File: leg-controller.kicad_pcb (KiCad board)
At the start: 2 copper layers, 99.8 x 77.5 mm, 103 parts, among them J1 Power, J10 Motor, J11 Rotary_Encoder, J12 Conn_01x02, J13 USB_B_Mini, J14 ISP, J15 Motor_E, J16 Motor_D, J17 Motor_F, J18 Conn_01x02, J19 Conn_01x02, J2 I2C, J3 Conn_02x01, J4 Motor, J5 Rotary_Encoder, J6 Conn_02x01, J7 Motor, J8 Rotary_Encoder, J9 Conn_02x01, Q1 Q_NPN_BEC, Q2 SiSS05DN, Q3 Q_NPN_BEC, Q4 SiSS05DN, Q5 Q_NPN_BEC, Q6 SiSS05DN, SW1 Function, U1 LD1117S33TR_SOT223, U2 ATmega644P-20PU, U3 OPA333xxDCK, U4 OPA333xxDCK, U5 OPA333xxDCK, Y1 12MHz

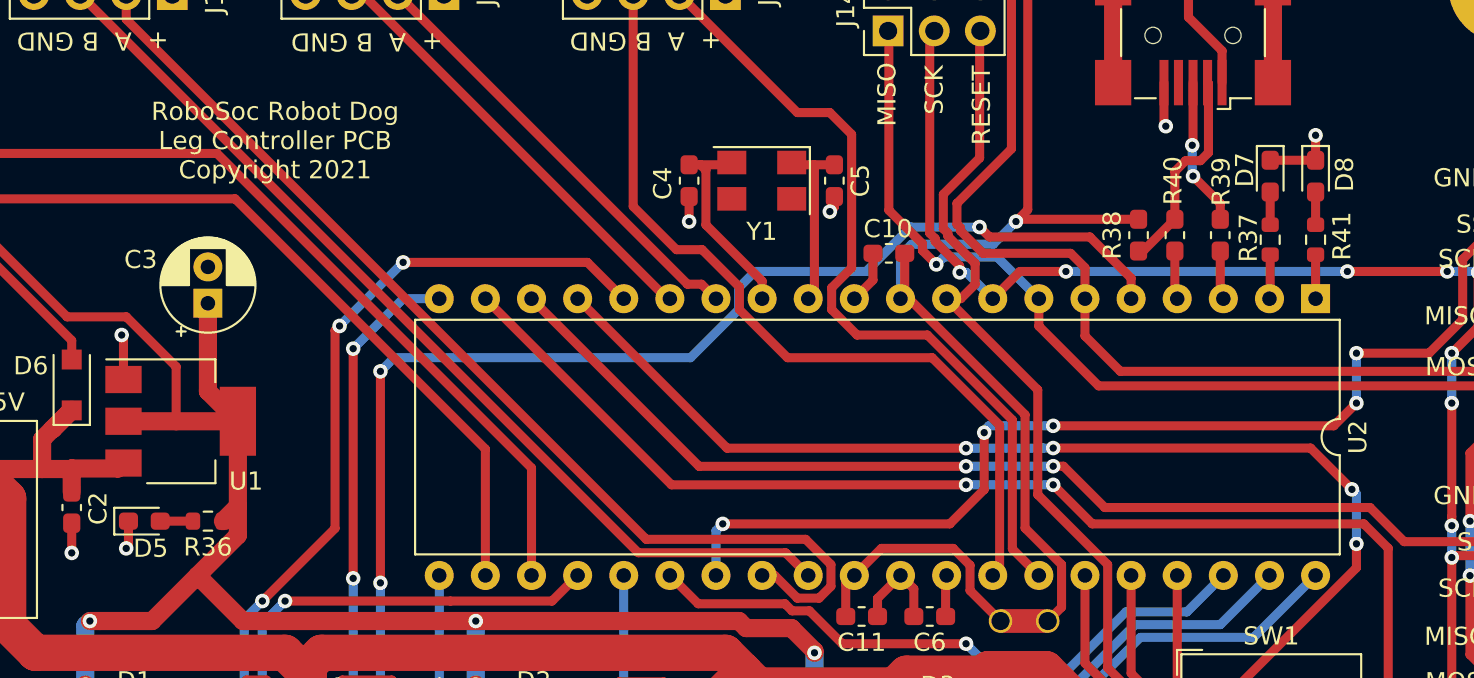
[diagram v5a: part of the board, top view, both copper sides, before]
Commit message: Added labels for LEDs
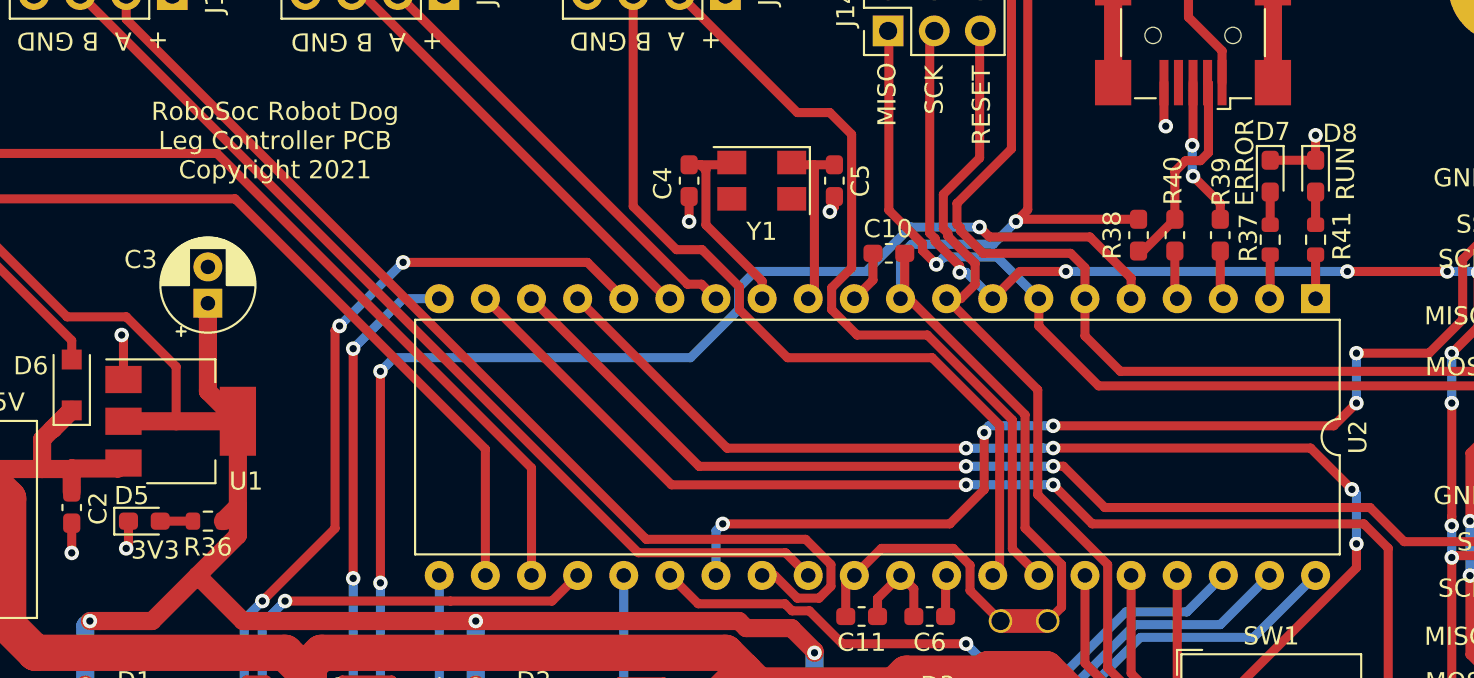
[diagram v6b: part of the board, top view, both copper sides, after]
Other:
- board text added: "ERROR"
- board text added: "RUN"
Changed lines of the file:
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@@
   (general
     (thickness 1.6)
-    (drawings 51)
+    (drawings 54)
     (tracks 938)
     (zones 0)
@@
     (tags "LED handsolder")
     (attr smd)
-    (fp_text reference D8 (at -0.1 -1.6 90) (layer F.SilkS)
+    (fp_text reference D8 (at -2.35 -1.35 180) (layer F.SilkS)
       (effects (font (size 1 1) (thickness 0.15)))
     )
@@
     (tags "LED handsolder")
     (attr smd)
-    (fp_text reference D7 (at -0.35 1.4 90) (layer F.SilkS)
+    (fp_text reference D7 (at -2.45 -0.15 180) (layer F.SilkS)
       (effects (font (size 1 1) (thickness 0.15)))
     )
@@
     (tags "LED handsolder")
     (attr smd)
-    (fp_text reference D5 (at 0.35 1.5) (layer F.SilkS)
+    (fp_text reference D5 (at -0.7 -1.4) (layer F.SilkS)
       (effects (font (size 1 1) (thickness 0.15)))
     )
@@
     )
   )
+  (gr_text ERROR (at 166.35 82 90) (layer F.SilkS)
+    (effects (font (size 1 1) (thickness 0.15)))
+  )
+  (gr_text RUN (at 171.9 82.6 90) (layer F.SilkS)
+    (effects (font (size 1 1) (thickness 0.15)))
+  )
+  (gr_text 3V3 (at 106.35 103.35) (layer F.SilkS)
+    (effects (font (size 1 1) (thickness 0.15)))
+  )
   (gr_text "Power: 4-15V" (at 94.6 95.2) (layer F.SilkS)
